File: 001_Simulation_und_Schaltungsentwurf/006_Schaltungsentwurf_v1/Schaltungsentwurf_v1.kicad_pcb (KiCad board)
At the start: 2 copper layers, 69 parts, among them IC1 MPY634KP, IC2 MPY634KP, IC3 MPY634KP, J1 Screw_Terminal_01x04, U1 TL082, U2 TL082, U3 MCP4261-104E_P, U4 MCP4261-104E_P, U5 TL082

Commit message: Stand 14.11
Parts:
- removed A1: RaspberryPi_Pico_W, 000_OUF:RaspberryPi_Pico_W_THT
- removed C7: 100uF, Capacitor_THT:C_Radial_D8.0mm_H11.5mm_P3.50mm
- removed C9: 1000uF, Capacitor_THT:C_Radial_D10.0mm_H16.0mm_P5.00mm
- removed D1: MBR360, 000_OUF:1N4001
- removed H1, H2, H3, H4: MountingHole, MountingHole:MountingHole_2.2mm_M2_DIN965
- removed J1: Screw_Terminal_01x04, 000_OUF:Terminal 4 Pol
- removed L1: 100uH, Inductor_THT:L_Radial_D8.7mm_P5.00mm_Fastron_07HCP
- removed PS1: LM2576WT, Package_TO_SOT_THT:TO-220-5_Vertical
- removed R7, R8: 1k, 000_OUF:Resistor
- removed RV6: 5k, 000_OUF:Trimmer Rund
- removed TP1: BPF, 000_OUF:TestPoint
- removed TP10: Vc, 000_OUF:TestPoint
- removed TP11: +15V, 000_OUF:TestPoint
- removed TP12: -15V, 000_OUF:TestPoint
- removed TP13: +3.3V, 000_OUF:TestPoint
- removed TP2: V_in, 000_OUF:TestPoint
- removed TP4: LPF, 000_OUF:TestPoint
- removed TP5: BSF, 000_OUF:TestPoint
- removed TP7: HPF, 000_OUF:TestPoint
- removed TP8: Vc_DC, 000_OUF:TestPoint
- removed TP9: GND, 000_OUF:TestPoint
- added C11: 100n, 000_OUF:100nF, F.Cu at (196.5, 88.4)
- added C12: 100n, 000_OUF:100nF, F.Cu at (196.4, 57.0)
- added C13: 100n, 000_OUF:100nF, F.Cu at (196.4, 72.3)
- C1, C3, C5: value {CCOM} -> 1u
- JP2: value SF1 -> ~
- JP3: value SF2 -> ~
- JP4: value SF3 -> ~
- R2, R3, R4, R5, R9: value {RCOM} -> 1k
- RV1, RV2, RV4, RV5: footprint 000_OUF:Trimmer Rund -> Potentiometer_THT:Potentiometer_Bourns_3296Y_Vertical
- RV3: footprint 000_OUF:Trimmer straight -> Potentiometer_THT:Potentiometer_Bourns_3296Y_Vertical
- TP6: value SHDN1 -> SHDN2
- moved RV5 149.0 mm to (248.3, 85.3)
- moved JP12 148.8 mm to (254.3, 125.3)
- moved RV4 146.5 mm to (237.6, 85.3)
- moved RV2 131.7 mm to (202.5, 55.8), turned to -90 degrees
- moved RV1 127.5 mm to (202.3, 87.2), turned to -90 degrees
- moved R9 123.0 mm to (239.1, 102.9)
- moved R11 97.1 mm to (214.9, 65.0), turned to -90 degrees
- moved R10 90.4 mm to (209.9, 77.7), turned to 90 degrees
- moved C5 78.8 mm to (241.2, 119.9)
- moved JP3 74.6 mm to (202.1, 60.5), turned to -90 degrees
- moved U5 67.8 mm to (184.5, 120.8), turned to 90 degrees
- moved IC1 67.6 mm to (178.0, 89.7), turned to 90 degrees
- moved RV3 63.7 mm to (202.2, 71.0), turned to -90 degrees
- moved JP6 63.5 mm to (127.5, 61.8), turned to 90 degrees
- moved JP2 60.7 mm to (201.8, 91.8), turned to -90 degrees
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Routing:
- net GND: track 0.00 -> 237.4 mm, vias 0 -> 5
- net +15V: track 0.00 -> 177.6 mm, vias 0 -> 1
- net HPF: track 0.00 -> 141.7 mm
- net -15V: track 0.00 -> 127.9 mm, vias 0 -> 3
- net +3.3V: track 0.00 -> 82.6 mm
- net BPF: track 0.00 -> 68.7 mm
- net MOSI: track 0.00 -> 60.2 mm, vias 0 -> 1
- net Vc: track 0.00 -> 58.9 mm, vias 0 -> 1
- net SCK: track 0.00 -> 58.8 mm, vias 0 -> 1
- net CS2: track 0.00 -> 49.3 mm, vias 0 -> 1
- net LPF: track 0.00 -> 46.7 mm, vias 0 -> 2
- net MISO: track 0.00 -> 43.5 mm, vias 0 -> 1
- net CS1: track 0.00 -> 31.9 mm
- net Net-(JP9-B): track 0.00 -> 29.0 mm
- net RQ_out: track 0.00 -> 27.1 mm
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- added copper zone on B.Cu, net GND
- added copper zone on F.Cu, net GND
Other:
- board outline added: 176.1 x 97.4 mm

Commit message: Erste Iteration des PCBs
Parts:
- added A1: RaspberryPi_Pico_W, 000_OUF:RaspberryPi_Pico_W_THT, F.Cu at (94.0, 106.2)
- added C7: 470uF, Capacitor_THT:C_Radial_D10.0mm_H16.0mm_P5.00mm, F.Cu at (214.8, 101.0)
- added C9: 330uF, Capacitor_THT:C_Radial_D10.0mm_H16.0mm_P5.00mm, F.Cu at (195.5, 105.2)
- added D1: 1N5820, Diode_THT:D_DO-27_P15.24mm_Horizontal, F.Cu at (209.8, 124.1)
- added G***: LOGO, AQUA-link_bib:HSB_Logo, F.Cu at (117.9, 122.5)
- added H1: MountingHole, MountingHole:MountingHole_2.2mm_M2_DIN965, F.Cu at (77.1, 53.8)
- added H2: MountingHole, MountingHole:MountingHole_2.2mm_M2_DIN965, F.Cu at (215.7, 53.8)
- added H3: MountingHole, MountingHole:MountingHole_2.2mm_M2_DIN965, F.Cu at (77.1, 128.5)
- added H4: MountingHole, MountingHole:MountingHole_2.2mm_M2_DIN965, F.Cu at (215.7, 128.5)
- added J1: Screw_Terminal_01x04, 000_OUF:Terminal 4 Pol, F.Cu at (120.5, 54.2)
- added J2: Conn_Coaxial, 001_CNC:BNC Edge Mount, F.Cu at (187.3, 127.1)
- added J3: Conn_Coaxial, 001_CNC:BNC Edge Mount, F.Cu at (171.0, 127.1)
- added J4: Conn_Coaxial, 001_CNC:BNC Edge Mount, F.Cu at (138.3, 127.1)
- added J5: Conn_Coaxial, 001_CNC:BNC Edge Mount, F.Cu at (154.7, 127.1)
- added J6: Conn_Coaxial, 001_CNC:BNC Edge Mount, F.Cu at (121.9, 127.1)
- added JP13: ~, 000_OUF:Connector 2 Pin 2.54mm, F.Cu at (176.8, 119.1)
- added L1: 68uH, Inductor_THT:L_Radial_D12.0mm_P5.00mm_Fastron_11P, F.Cu at (186.0, 119.3)
- added R7: 1k, 000_OUF:Resistor, F.Cu at (161.8, 112.4)
- added R8: 1k, 000_OUF:Resistor, F.Cu at (174.4, 108.4)
- added Ref**: Val**, 003_logos:QR_GitHub, F.Cu at (88.0, 61.1)
- added TP1: BPF, 000_OUF:TestPoint, F.Cu at (138.1, 115.1)
- added TP10: Vc, 000_OUF:TestPoint, F.Cu at (208.4, 58.5)
- added TP11: +15V, 000_OUF:TestPoint, F.Cu at (120.5, 61.1)
- added TP12: -15V, 000_OUF:TestPoint, F.Cu at (105.2, 61.2)
- added TP13: +3.3V, 000_OUF:TestPoint, F.Cu at (118.0, 88.4)
- added TP14: ZCD, 000_OUF:TestPoint, F.Cu at (108.9, 110.0)
- added TP15: FFT, 000_OUF:TestPoint, F.Cu at (109.0, 104.9)
- added TP16: mult1_out, 000_OUF:TestPoint, F.Cu at (150.0, 102.4)
- added TP17: mult2_out, 000_OUF:TestPoint, F.Cu at (195.3, 52.8)
- added TP18: mult3_out, 000_OUF:TestPoint, F.Cu at (171.5, 72.1)
- added TP2: V_in, 000_OUF:TestPoint, F.Cu at (132.1, 115.1)
- added TP4: LPF, 000_OUF:TestPoint, F.Cu at (150.1, 115.1)
- added TP5: BSF, 000_OUF:TestPoint, F.Cu at (144.1, 115.1)
- added TP7: HPF, 000_OUF:TestPoint, F.Cu at (156.1, 115.1)
- added TP8: Vc_DC, 000_OUF:TestPoint, F.Cu at (215.0, 58.5)
- added TP9: GND, 000_OUF:TestPoint, F.Cu at (126.1, 115.1)
- added U6: LM2596T-3.3, Package_TO_SOT_THT:TO-220-5_P3.4x3.7mm_StaggerOdd_Lead3.8mm_Vertical, F.Cu at (205.2, 121.0)
- JP1: value ~ -> R1_in
- JP10: value ~ -> RQ_out
- JP11: value ~ -> RH0_out
- JP5: value ~ -> R1_out
- JP6: value ~ -> R2_in
- JP7: value ~ -> RQ_in
- JP8: value ~ -> RH0_in
- JP9: value ~ -> R2_out
- R10, R11: value {RCOM} -> 1k
- moved R9 79.0 mm to (160.1, 103.2)
- moved C5 71.5 mm to (172.7, 99.3), turned to 90 degrees
- moved JP12 60.9 mm to (211.1, 82.3)
- moved RV5 42.5 mm to (205.9, 87.3), turned to 90 degrees
- moved U5 24.9 mm to (178.2, 96.8), turned to 0 degrees
- moved RV4 22.5 mm to (216.2, 92.2), turned to -90 degrees
- moved C3 13.6 mm to (151.6, 65.7), turned to -90 degrees
- moved C10 12.9 mm to (184.5, 107.7), turned to 180 degrees
- moved JP10 11.1 mm to (149.2, 83.0)
- moved JP11 10.8 mm to (149.2, 89.0)
- moved R4 10.8 mm to (169.5, 88.7), turned to 180 degrees
- moved C6 9.43 mm to (159.4, 55.3), turned to 0 degrees
- moved U1 8.79 mm to (165.7, 66.5), turned to 180 degrees
- moved U2 6.89 mm to (167.0, 76.9)
- moved C8 6.80 mm to (155.8, 83.2)
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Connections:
- net /BSF renamed BSF
- RV1 pad 3: -10V -> -15V
- RV2 pad 3: -10V -> -15V
- RV3 pad 3: -10V -> -15V
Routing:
- net -15V: track 127.9 -> 326.5 mm, vias 3 -> 2
- net GND: track 237.4 -> 404.9 mm, vias 5 -> 10
- net V_in: track 0.00 -> 159.2 mm
- net +15V: track 177.6 -> 308.7 mm, vias 1 -> 2
- net BPF: track 68.7 -> 176.5 mm, vias 0 -> 2
- net /ZCD: track 0.00 -> 103.6 mm, vias 0 -> 2
- net +3.3V: track 82.6 -> 175.4 mm, vias 0 -> 1
- net BSF: track 11.7 -> 85.5 mm
- net LPF: track 46.7 -> 116.3 mm, vias 2 -> 0
- net CS1: track 31.9 -> 94.6 mm, vias 0 -> 2
- net SCK: track 58.8 -> 118.1 mm, vias 1 -> 3
- net Net-(C5-Pad2): track 0.00 -> 58.6 mm
- net CS2: track 49.3 -> 107.6 mm, vias 1 -> 2
- net MOSI: track 60.2 -> 112.9 mm, vias 1 -> 2
- net mult1_out: track 2.54 -> 48.5 mm
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- added copper zone on In2.Cu, net +15V
- added copper zone on In1.Cu, net GND
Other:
- board size 176.1 x 97.4 mm -> 146 x 82.1 mm
- copper layers 2 -> 4
- board text added: "Nils Renner"
- board text added: "Nils Renner Self-Tuned Biquad-Filter"
- board text added: "Self-Tuned Biquad-Filter"

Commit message: documentation of the PCB (iteration 1)
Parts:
- removed the Ref** at (88.0, 61.1)
- added Ref**: Val**, 003_logos:git_qr, F.Cu at (89.9, 66.6)
- added Ref**: Val**, 003_logos:logo_nils, B.Cu at (89.9, 66.6)
- moved TP17 10.0 mm to (205.3, 52.8)
- moved C7 0.74 mm to (214.8, 101.7)
- moved RV4 0.06 mm to (216.2, 92.3)
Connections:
- A1 pad 36: +3.3V -> unconnected-(A1-3V3-Pad36)
- A1 pad 39: unconnected-(A1-VSYS-Pad39) -> +3.3V
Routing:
- net GND: track 404.9 -> 598.8 mm
- net V_in: track 159.2 -> 148.2 mm
- net mult2_out: track 30.9 -> 40.9 mm
- net +3.3V: track 175.4 -> 167.3 mm
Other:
- board text added: "Version 1"

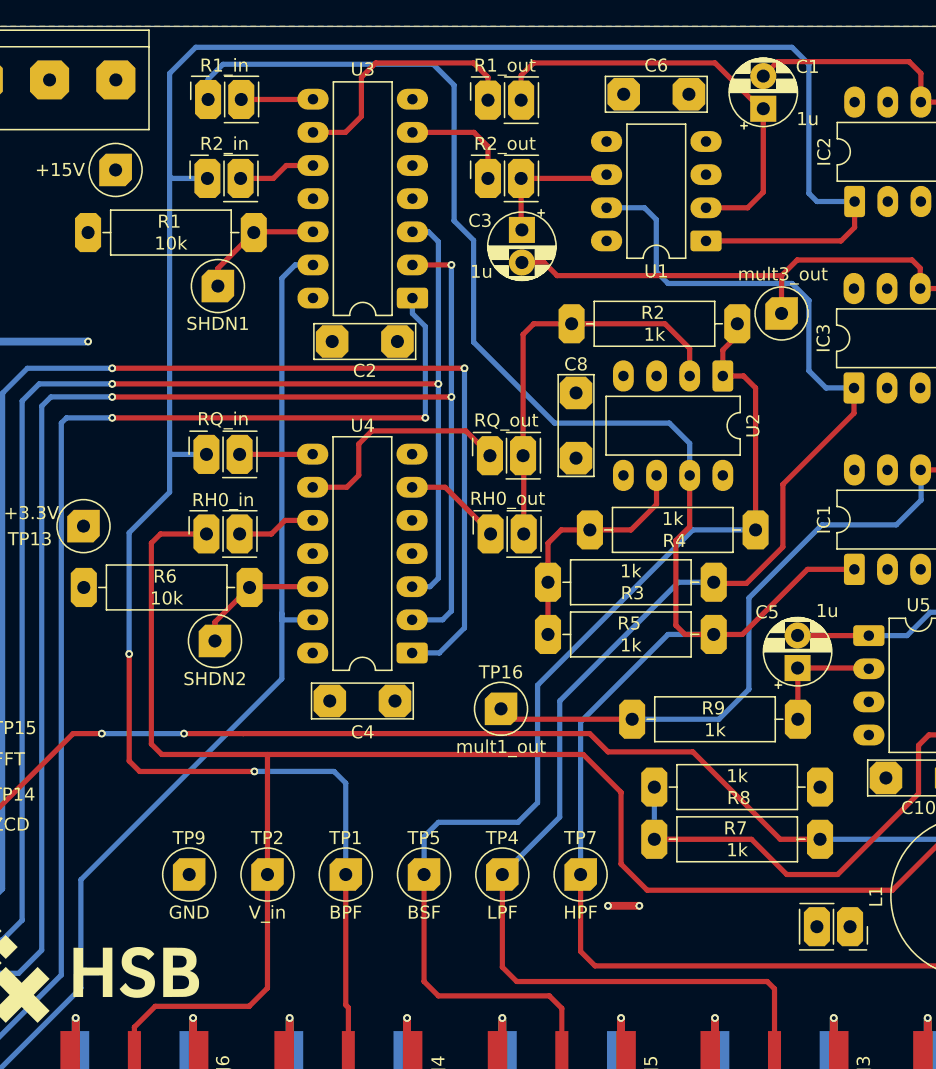
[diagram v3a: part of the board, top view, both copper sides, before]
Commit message: Konflikt aufgelöst: Theorie_neu.tex übernommen
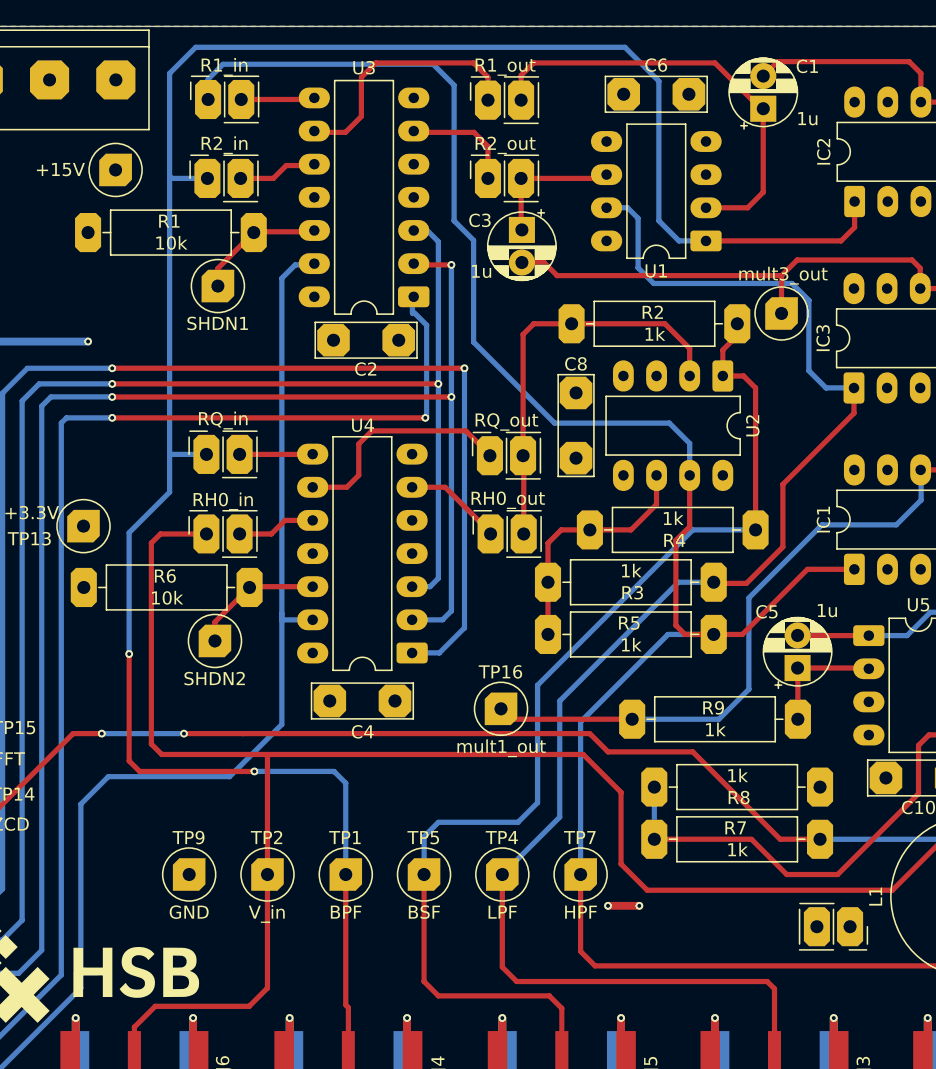
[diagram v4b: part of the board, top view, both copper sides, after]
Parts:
- moved U3 0.14 mm to (143.3, 70.8)
- moved C2 0.14 mm to (137.2, 74.2)
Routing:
- net BPF: track 176.5 -> 166.9 mm
- net MISO: track 83.2 -> 88.7 mm
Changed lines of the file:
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@@
 	(footprint "000_OUF:100nF"
 		(layer "F.Cu")
-		(at 137.06 74.25)
+		(at 137.16 74.15)
 		(property "Reference" "C2"
 			(at 3.048 -2.54 0)
@@
 	(footprint "000_OUF:DIP_14"
 		(layer "F.Cu")
-		(at 143.21 70.92 180)
+		(at 143.31 70.82 180)
 		(descr "14-lead though-hole mounted DIP package, row spacing 7.62mm (300 mils), LongPads")
 		(tags "THT DIP DIL PDIP 2.54mm 7.62mm 300mil LongPads")
@@
 	(segment
 		(start 147.2 76.3)
-		(end 120.2 76.3)
+		(end 120.4 76.3)
 		(width 0.4)
 		(layer "F.Cu")
@@
 	)
 	(segment
-		(start 133.2 95.1)
-		(end 133.2 100.1)
+		(start 133.2 103.6)
+		(end 129.2 107.6)
 		(width 0.4)
 		(layer "B.Cu")
@@
 	)
 	(segment
-		(start 117.8 115.5)
+		(start 117.8 109.7)
 		(end 117.8 123.8)
 		(width 0.4)
@@
 	)
 	(segment
+		(start 133.2 95.1)
+		(end 133.2 103.6)
+		(width 0.4)
+		(layer "B.Cu")
+		(net 5)
+	)
+	(segment
 		(start 133.2 95.58)
 		(end 133.2 95.1)
@@
 	)
 	(segment
-		(start 134.22 68.38)
-		(end 135.59 68.38)
+		(start 119.9 107.6)
+		(end 117.8 109.7)
 		(width 0.4)
 		(layer "B.Cu")
@@
 	)
 	(segment
-		(start 133.2 100.1)
-		(end 117.8 115.5)
+		(start 134.22 68.38)
+		(end 135.59 68.38)
 		(width 0.4)
 		(layer "B.Cu")
@@
 	)
 	(segment
+		(start 111.3075 130.2925)
+		(end 103.69 130.2925)
+		(width 0.4)
+		(layer "B.Cu")
+		(net 5)
+	)
+	(segment
 		(start 133.2 95.1)
 		(end 133.2 69.4)
@@
 	)
 	(segment
-		(start 111.3075 130.2925)
-		(end 103.69 130.2925)
+		(start 129.2 107.6)
+		(end 119.9 107.6)
 		(width 0.4)
 		(layer "B.Cu")
@@
 	)
 	(segment
-		(start 144.2 80.1)
-		(end 144.2 73.1)
+		(start 144.3 80)
+		(end 144.3 73)
 		(width 0.4)
 		(layer "B.Cu")
@@
 	)
 	(segment
-		(start 144.2 73.1)
-		(end 143.21 72.11)
+		(start 144.3 73)
+		(end 143.31 72.01)
 		(width 0.4)
 		(layer "B.Cu")
@@
 	)
 	(segment
-		(start 174.22 63.52)
+		(start 177.08 63.5)
 		(end 177.1 63.52)
 		(width 0.4)
@@
 	)
 	(segment
-		(start 173.6 62.9)
-		(end 174.22 63.52)
+		(start 163.64 66.54)
+		(end 165.71 66.54)
 		(width 0.4)
 		(layer "B.Cu")
@@
 	)
 	(segment
-		(start 137.2 107.2)
-		(end 138.1 108.1)
+		(start 162.1 65)
+		(end 163.64 66.54)
 		(width 0.4)
 		(layer "B.Cu")
@@
 	)
 	(segment
-		(start 173.6 53)
-		(end 173.6 62.9)
+		(start 162.1 54.3)
+		(end 162.1 65)
 		(width 0.4)
 		(layer "B.Cu")
@@
 	)
 	(segment
-		(start 172.3 51.7)
-		(end 173.6 53)
+		(start 137.2 107.2)
+		(end 138.1 108.1)
 		(width 0.4)
 		(layer "B.Cu")
@@
 	)
 	(segment
+		(start 126.6 51.7)
+		(end 159.5 51.7)
+		(width 0.4)
+		(layer "B.Cu")
+		(net 26)
+	)
+	(segment
 		(start 124.6 82.9)
 		(end 124.6 61.7)
@@
 	)
 	(segment
+		(start 159.5 51.7)
+		(end 162.1 54.3)
+		(width 0.4)
+		(layer "B.Cu")
+		(net 26)
+	)
+	(segment
 		(start 138.1 108.1)
 		(end 138.1 115.1)
@@
 	)
 	(segment
-		(start 124.6 53.7)
-		(end 126.6 51.7)
+		(start 124.6 61.7)
+		(end 124.6 53.7)
 		(width 0.4)
 		(layer "B.Cu")
@@
 	)
 	(segment
-		(start 124.6 61.7)
-		(end 124.6 53.7)
+		(start 124.6 53.7)
+		(end 126.6 51.7)
 		(width 0.4)
 		(layer "B.Cu")
@@
 	)
 	(segment
-		(start 126.6 51.7)
-		(end 172.3 51.7)
-		(width 0.4)
-		(layer "B.Cu")
-		(net 26)
-	)
-	(segment
 		(start 124.6 82.9)
 		(end 124.6 85.8)
@@
 	)
 	(segment
-		(start 166.3 92.7)
-		(end 163.6 92.7)
+		(start 158.09 64)
+		(end 159.7 64)
 		(width 0.4)
 		(layer "B.Cu")
@@
 	)
 	(segment
-		(start 154.5 101.8)
-		(end 154.5 110.7)
+		(start 160.5 68.6)
+		(end 161.7 69.8)
 		(width 0.4)
 		(layer "B.Cu")
@@
 	)
 	(segment
-		(start 172.3 69.8)
-		(end 173.6 71.1)
+		(start 160.5 64.8)
+		(end 160.5 68.6)
 		(width 0.4)
 		(layer "B.Cu")
@@
 	)
 	(segment
-		(start 161.9 64.9)
-		(end 161.9 68.9)
+		(start 166.3 92.7)
+		(end 163.6 92.7)
 		(width 0.4)
 		(layer "B.Cu")
@@
 	)
 	(segment
-		(start 162.8 69.8)
-		(end 172.3 69.8)
+		(start 154.5 101.8)
+		(end 154.5 110.7)
 		(width 0.4)
 		(layer "B.Cu")
@@
 	)
 	(segment
-		(start 158.09 64)
-		(end 161 64)
+		(start 159.7 64)
+		(end 160.5 64.8)
 		(width 0.4)
 		(layer "B.Cu")
@@
 	)
 	(segment
-		(start 154.5 110.7)
-		(end 150.1 115.1)
+		(start 172.3 69.8)
+		(end 173.6 71.1)
 		(width 0.4)
 		(layer "B.Cu")
@@
 	)
 	(segment
-		(start 161 64)
-		(end 161.9 64.9)
+		(start 154.5 110.7)
+		(end 150.1 115.1)
 		(width 0.4)
 		(layer "B.Cu")
@@
 	)
 	(segment
-		(start 161.9 68.9)
-		(end 162.8 69.8)
+		(start 173.6 71.1)
+		(end 173.6 76.5)
 		(width 0.4)
 		(layer "B.Cu")
@@
 	)
 	(segment
-		(start 173.6 71.1)
-		(end 173.6 76.5)
+		(start 161.7 69.8)
+		(end 172.3 69.8)
 		(width 0.4)
 		(layer "B.Cu")
@@
 	)
 	(zone
-		(net 3)
-		(net_name "+3.3V")
+		(net 15)
+		(net_name "-15V")
 		(layer "In2.Cu")
 		(name "$teardrop_padvia$")
 		(hatch none 0.1)
-		(priority 30015)
+		(priority 30010)
 		(attr
 			(teardrop
@@
 		(polygon
 			(pts
-				(xy 136.76 76.5) (xy 137.36 76.5) (xy 138.06 75.25) (xy 137.06 74.249) (xy 136.06 75.25)
+				(xy 198.15 71.48) (xy 198.15 70.88) (xy 196.766607 70.366607) (xy 195.899 71.5) (xy 197.054162 72.345837)
 			)
 		)
@@
 		(name "$teardrop_padvia$")
 		(hatch none 0.1)
-		(priority 30014)
-		(attr
-			(teardrop
-				(type padvia)
-			)
-		)
-		(connect_pads yes
-			(clearance 0)
-		)
-		(min_thickness 0.0254)
-		(filled_areas_thickness no)
-		(fill yes
-			(thermal_gap 0.5)
-			(thermal_bridge_width 0.5)
-			(island_removal_mode 1)
-			(island_area_min 10)
-		)
-		(polygon
-			(pts
-				(xy 134.81 73.95) (xy 134.81 74.55) (xy 136.06 75.25) (xy 137.061 74.25) (xy 136.06 73.25)
-			)
-		)
-	)
-	(zone
-		(net 15)
-		(net_name "-15V")
-		(layer "In2.Cu")
-		(name "$teardrop_padvia$")
-		(hatch none 0.1)
-		(priority 30010)
+		(priority 30000)
 		(attr
 			(teardrop
@@
 		(polygon
 			(pts
-				(xy 198.15 71.48) (xy 198.15 70.88) (xy 196.766607 70.366607) (xy 195.899 71.5) (xy 197.054162 72.345837)
+				(xy 135.89 72.44468) (xy 135.29 72.44468) (xy 135.91 74.269351) (xy 137.16 74.151) (xy 137.367841 72.9)
 			)
 		)
@@
 		(name "$teardrop_padvia$")
 		(hatch none 0.1)
-		(priority 30004)
+		(priority 30002)
 		(attr
 			(teardrop
@@
 		(polygon
 			(pts
-				(xy 135.89 72.44468) (xy 135.29 72.44468) (xy 135.81 74.299287) (xy 137.06 74.251) (xy 137.331221 73)
+				(xy 117.725 95.6) (xy 118.325 95.6) (xy 119.025 94.2) (xy 118.025 93.099) (xy 117.025 94.2)
 			)
 		)
@@
 		(name "$teardrop_padvia$")
 		(hatch none 0.1)
-		(priority 30002)
+		(priority 30012)
 		(attr
 			(teardrop
@@
 		(polygon
 			(pts
-				(xy 117.725 95.6) (xy 118.325 95.6) (xy 119.025 94.2) (xy 118.025 93.099) (xy 117.025 94.2)
+				(xy 136.575 104.05) (xy 137.175 104.05) (xy 137.875 102.8) (xy 136.875 101.799) (xy 135.875 102.8)
 			)
 		)
@@
 		(name "$teardrop_padvia$")
 		(hatch none 0.1)
-		(priority 30012)
+		(priority 30001)
 		(attr
 			(teardrop
@@
 		(polygon
 			(pts
-				(xy 136.575 104.05) (xy 137.175 104.05) (xy 137.875 102.8) (xy 136.875 101.799) (xy 135.875 102.8)
+				(xy 136.76 76.4) (xy 137.36 76.4) (xy 138.114495 75.195504) (xy 137.16 74.149) (xy 136.116477 75.106477)
 			)
 		)
@@
 			)
 		)
+	)
+	(zone
+		(net 3)
+		(net_name "+3.3V")
+		(layer "In2.Cu")
+		(name "$teardrop_padvia$")
+		(hatch none 0.1)
+		(priority 30002)
+		(attr
+			(teardrop
+				(type padvia)
+			)
+		)
+		(connect_pads yes
+			(clearance 0)
+		)
+		(min_thickness 0.0254)
+		(filled_areas_thickness no)
+		(fill yes
+			(thermal_gap 0.5)
+			(thermal_bridge_width 0.5)
+			(island_removal_mode 1)
+			(island_area_min 10)
+		)
+		(polygon
+			(pts
+				(xy 134.91 73.95) (xy 134.91 74.55) (xy 136.203522 75.193522) (xy 137.161 74.15) (xy 136.114495 73.195504)
+			)
+		)
